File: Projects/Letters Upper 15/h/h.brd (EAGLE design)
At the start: 16.5 x 21.6 mm, 42 parts

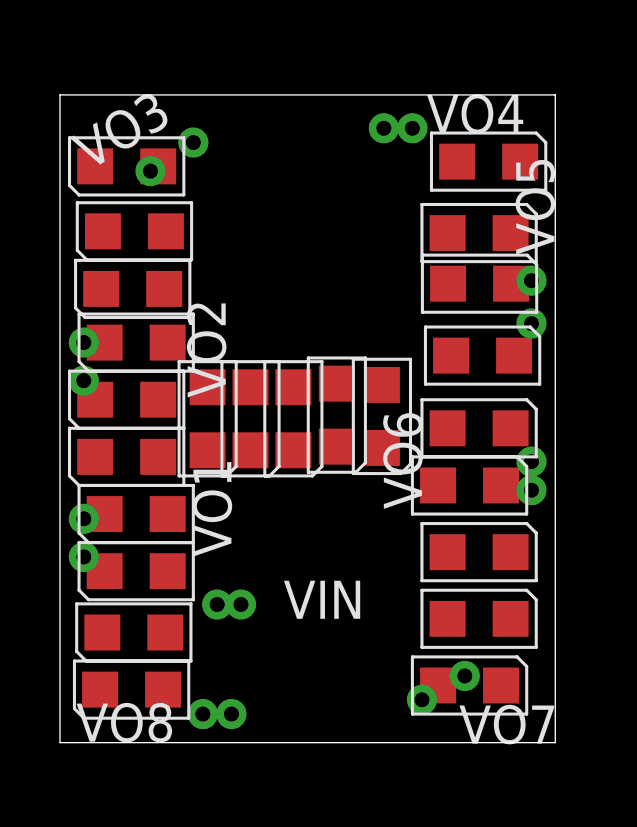
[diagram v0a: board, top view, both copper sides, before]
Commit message: 
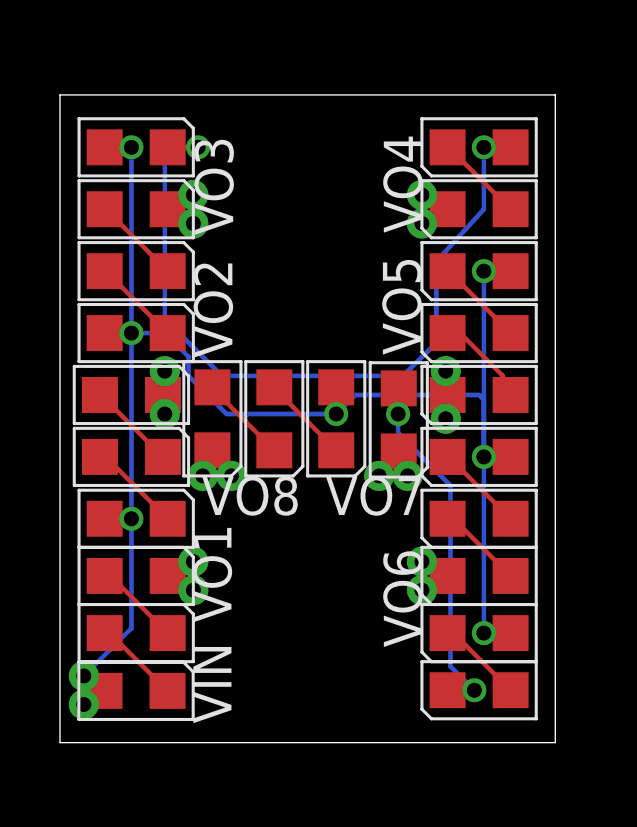
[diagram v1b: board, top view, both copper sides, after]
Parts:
- moved LED20 9.69 mm to (14.0, 1.75), turned to 90 degrees
- moved VO16 7.94 mm to (4.76, 8.89)
- moved VO8 7.94 mm to (5.71, 8.89)
- moved VO15 7.48 mm to (11.6, 8.89)
- moved VO7 7.25 mm to (10.6, 8.89)
- moved VIN1 6.21 mm to (0.79, 1.27)
- moved VIN 5.04 mm to (0.79, 2.22)
- moved VO14 4.94 mm to (12.1, 6.03)
- moved VO6 4.94 mm to (12.1, 5.08)
- moved VO13 4.27 mm to (12.9, 10.8)
- moved VO5 4.15 mm to (12.9, 12.4)
- moved VO1 3.92 mm to (4.45, 6.03)
- moved VO9 3.82 mm to (4.45, 5.08)
- moved VO10 3.60 mm to (3.49, 11.0)
- moved VO12 3.42 mm to (12.1, 17.3)
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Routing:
- net VIN: track 0.00 -> 53.8 mm, vias 0 -> 7
- net N$16: track 0.00 -> 26.2 mm, vias 0 -> 2
- net N$27: track 0.00 -> 12.0 mm, vias 0 -> 2
- net N$19: track 0.00 -> 3.18 mm
- net N$8: track 0.00 -> 3.11 mm
- net N$2: track 0.00 -> 2.95 mm
- net N$1: track 0.00 -> 2.95 mm
- net N$24: track 0.00 -> 2.95 mm
- net N$20: track 0.00 -> 2.95 mm
- net N$12: track 0.00 -> 2.95 mm
- net N$11: track 0.00 -> 2.95 mm
- net N$15: track 0.00 -> 2.95 mm
- net N$7: track 0.00 -> 2.95 mm
- net N$4: track 0.00 -> 2.89 mm
- net N$3: track 0.00 -> 2.89 mm
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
